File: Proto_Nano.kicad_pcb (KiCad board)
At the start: 2 copper layers, 43.2 x 17.8 mm, 32 parts, among them J1 USB_OTG, J2 ICSP_Header, SW1 RESET, U1 LM1117-5.0, U2 CH340G, U3 ATMEGA328P-AU, Y1 12MHz, Y2 16MHz

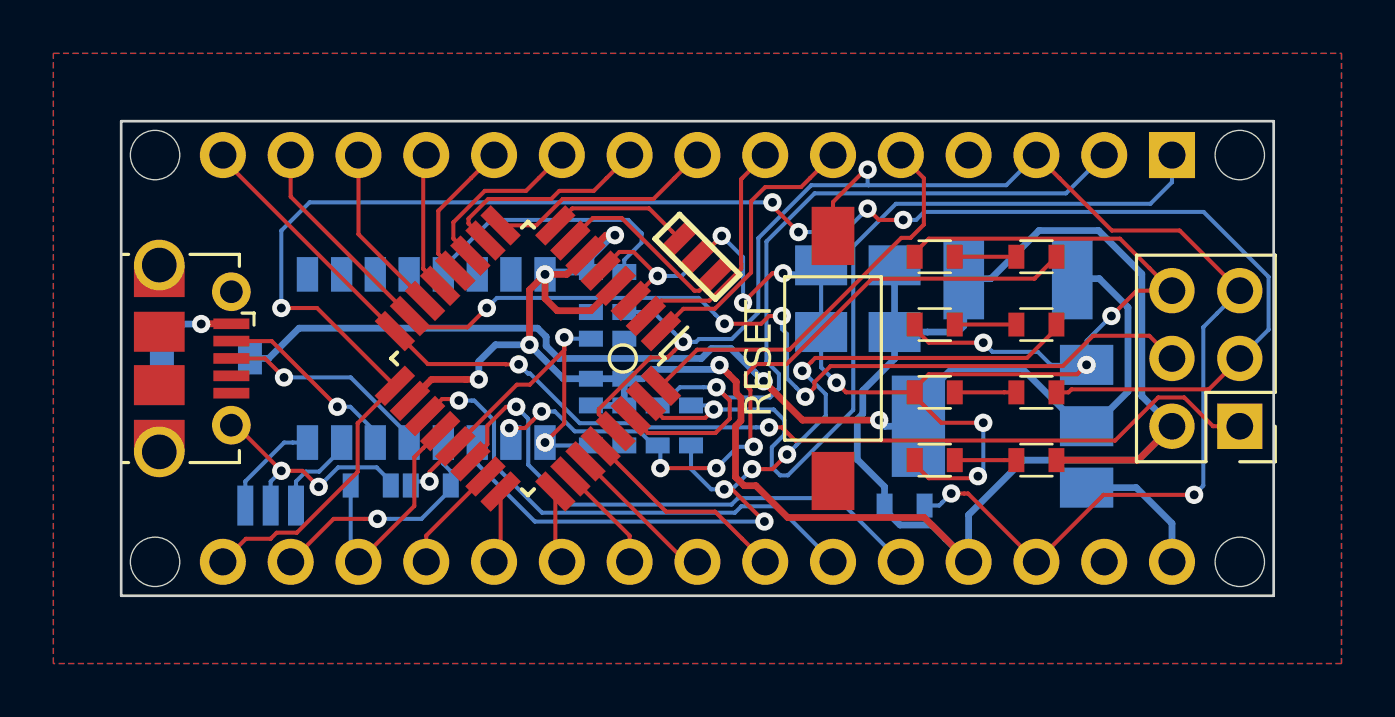
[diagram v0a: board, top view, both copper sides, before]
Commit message: move a via so it's not blocking some silkscreen text
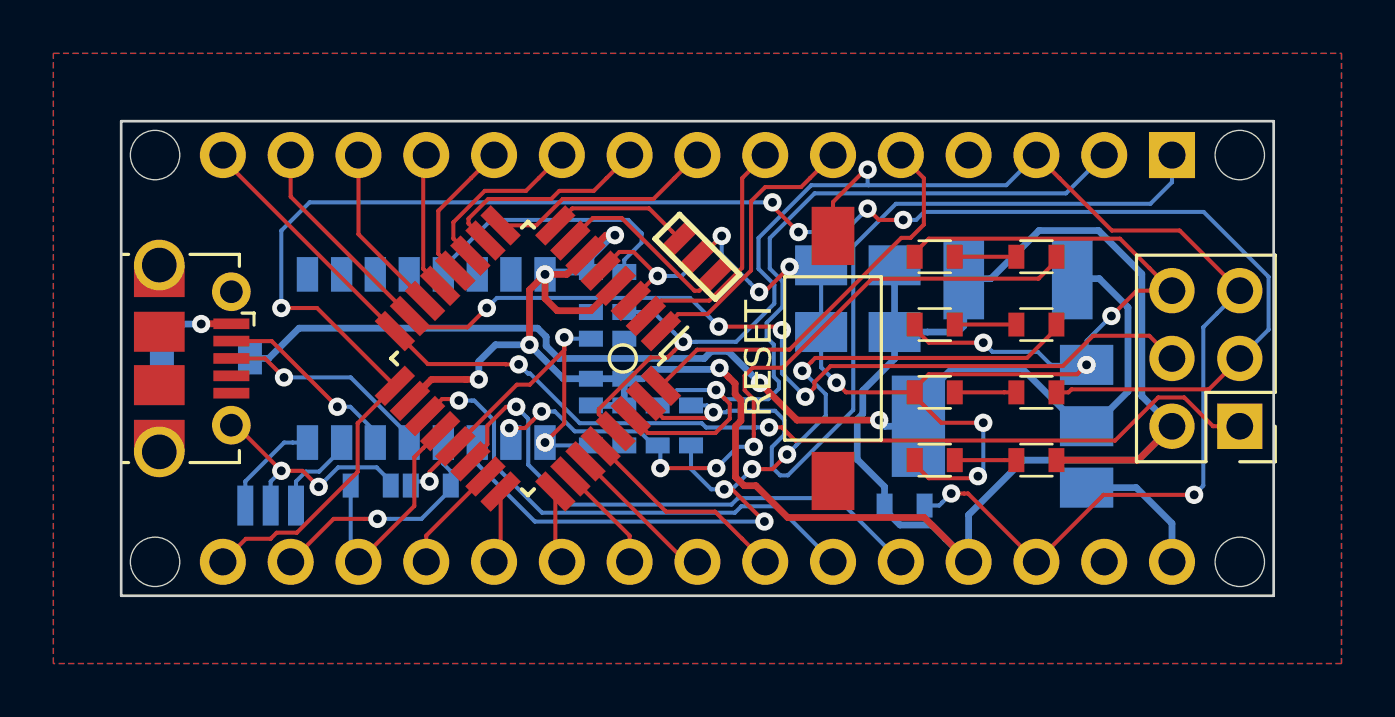
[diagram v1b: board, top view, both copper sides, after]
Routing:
- net GND: track 84.9 -> 84.0 mm
- net RESET: track 59.9 -> 60.5 mm
- net D11/MOSI: track 41.5 -> 41.0 mm

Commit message: zip gerbers and finish assembly diagram
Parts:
- Y1, Y2: footprint Polymetric_Resonators_SMD:murata-resonator_SMD_CSTCE16M0V53-R0 -> Polymetric_Resonators_SMD:1.3x3.2_resonator
